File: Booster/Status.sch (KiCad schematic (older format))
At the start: 33 parts, among them J601 StatusLED, P601 ~OVERCURRENT_OUT, P602 ~OVERCURRENT_OUT_OP, P603 MSTR_SW, P604 MSTR_SW_OUT, P605 MSTR_SW_OUT_OP, P606 ~DRIVER_ENABLE_OUT_OP, P607 ~DRIVER_ENABLE_OUT, Q601 BC807-40, Q602 BC807-40, Q603 BC807-40, Q604 BC817-40, SW601 MSTR_SW, U504 74HC08, U602 PC817, U603 PC817, U604 PC817

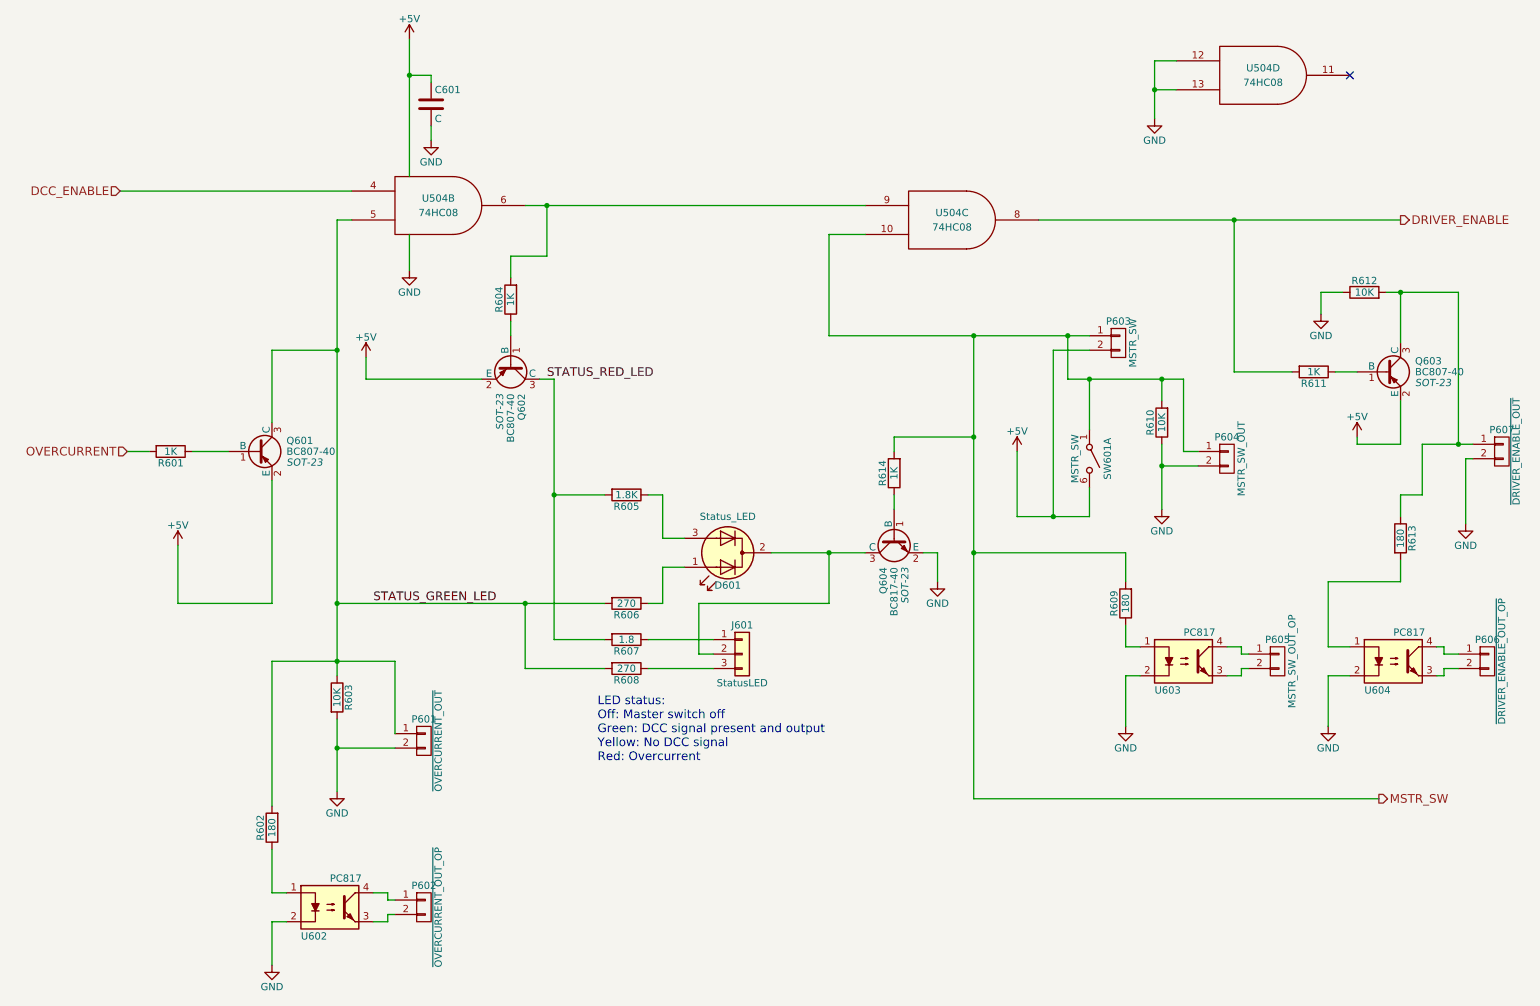
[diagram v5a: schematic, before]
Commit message: Assigned footprints & minor adjustments.
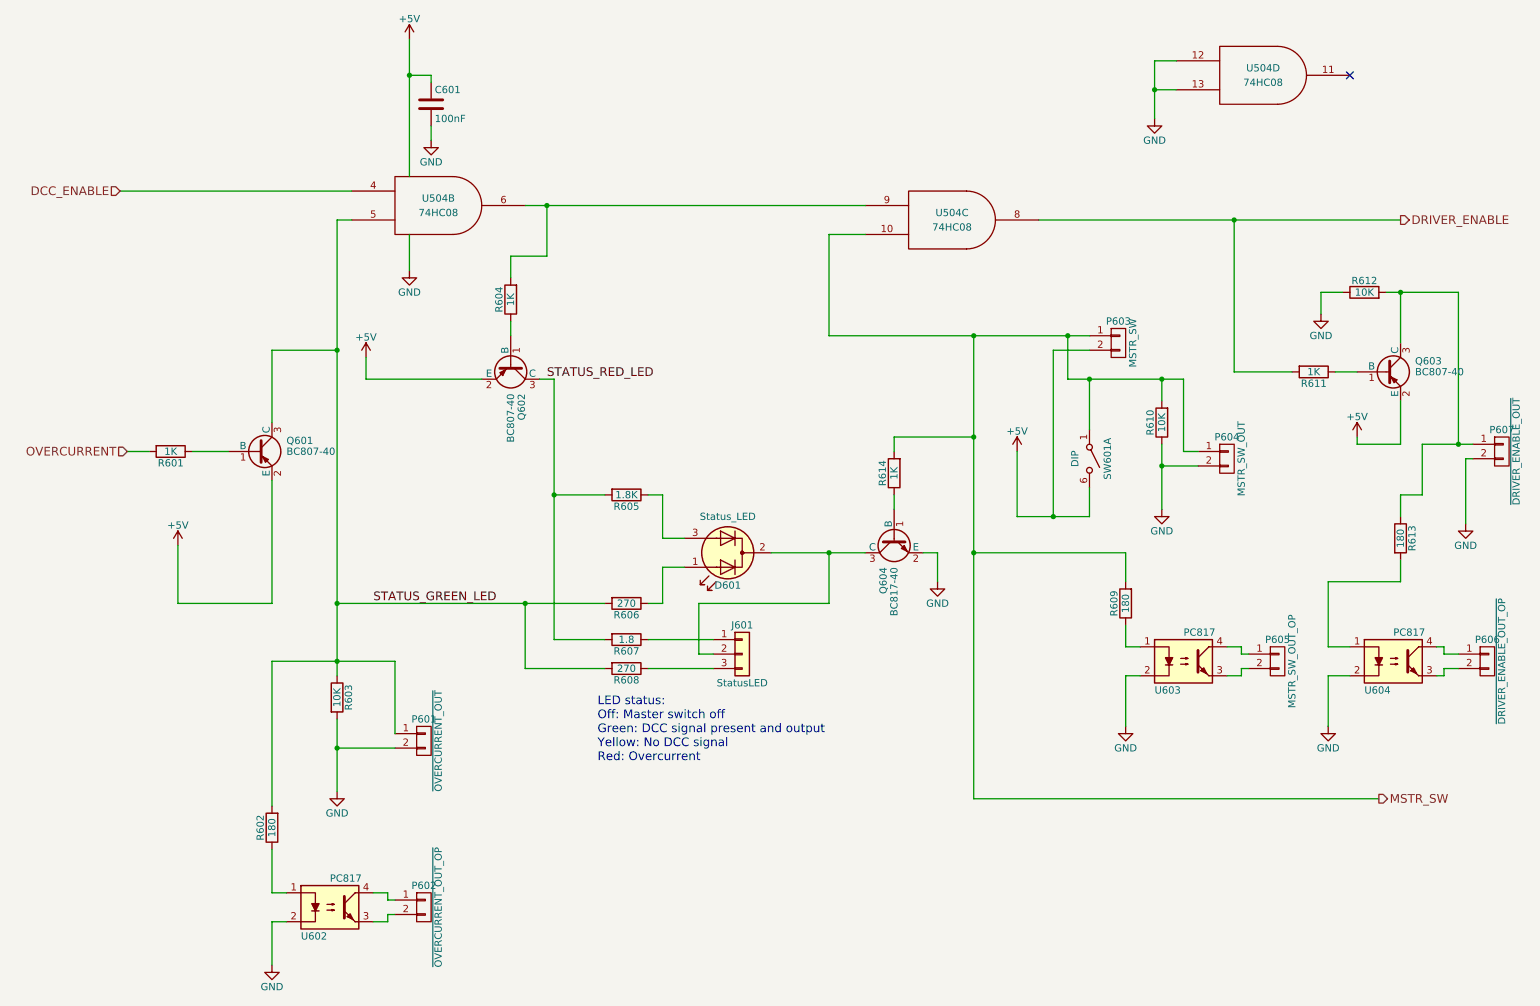
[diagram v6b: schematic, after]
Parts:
- C601: value C -> 100nF; footprint (none) -> Capacitors_SMD:C_0805
- D601: footprint (none) -> LEDs:LED_D3.0mm-3
- J601: footprint (none) -> Connectors_JST:JST_XH_B03B-XH-A_03x2.50mm_Straight
- P601, P602, P603, P604, P605, P606, P607: footprint (none) -> Connectors_JST:JST_XH_B02B-XH-A_02x2.50mm_Straight
- Q601, Q602, Q603, Q604: footprint SOT-23 -> TO_SOT_Packages_SMD:SOT-23
- R601, R602, R603, R604, R605, R606, R607, R608, R609, R610, R611, R612, R613, R614: footprint (none) -> Resistors_SMD:R_0805
- SW601: value MSTR_SW -> DIP; footprint (none) -> Buttons_Switches_THT:SW_DIP_x3_W7.62mm_Slide
- U504: footprint (none) -> SMD_Packages:SOIC-14_N

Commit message: Starting to add traces. Minor schematic changes to aid routing.
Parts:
- U602, U603, U604: footprint Housings_DIP:DIP-4_W7.62mm -> Housings_DIP:SMDIP-4_W9.53mm_Clearance8mm
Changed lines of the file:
@@
 $EndComp
 $Comp
-L +5V #PWR039
+L +5V #PWR609
 U 1 1 5A093F5C
 P 7600 3650
-F 0 "#PWR039" H 7600 3500 50  0001 C CNN
+F 0 "#PWR609" H 7600 3500 50  0001 C CNN
 F 1 "+5V" H 7600 3790 50  0000 C CNN
 F 2 "" H 7600 3650 50  0001 C CNN
@@
 $EndComp
 $Comp
-L +5V #PWR040
+L +5V #PWR601
 U 1 1 5A0BE54E
 P 1800 4300
-F 0 "#PWR040" H 1800 4150 50  0001 C CNN
+F 0 "#PWR601" H 1800 4150 50  0001 C CNN
 F 1 "+5V" H 1800 4440 50  0000 C CNN
 F 2 "" H 1800 4300 50  0001 C CNN
@@
 $EndComp
 $Comp
-L GND #PWR041
+L GND #PWR616
 U 1 1 5A0E0264
 P 10700 4150
-F 0 "#PWR041" H 10700 3900 50  0001 C CNN
+F 0 "#PWR616" H 10700 3900 50  0001 C CNN
 F 1 "GND" H 10700 4000 50  0000 C CNN
 F 2 "" H 10700 4150 50  0001 C CNN
@@
 $EndComp
 $Comp
-L +5V #PWR042
+L +5V #PWR615
 U 1 1 5A0E94CC
 P 9950 3550
-F 0 "#PWR042" H 9950 3400 50  0001 C CNN
+F 0 "#PWR615" H 9950 3400 50  0001 C CNN
 F 1 "+5V" H 9950 3690 50  0000 C CNN
 F 2 "" H 9950 3550 50  0001 C CNN
@@
 $EndComp
 $Comp
-L GND #PWR043
+L GND #PWR613
 U 1 1 5A0E9688
 P 9700 2700
-F 0 "#PWR043" H 9700 2450 50  0001 C CNN
+F 0 "#PWR613" H 9700 2450 50  0001 C CNN
 F 1 "GND" H 9700 2550 50  0000 C CNN
 F 2 "" H 9700 2700 50  0001 C CNN
@@
 $EndComp
 $Comp
-L GND #PWR044
+L GND #PWR603
 U 1 1 5A0E995B
 P 2900 6000
-F 0 "#PWR044" H 2900 5750 50  0001 C CNN
+F 0 "#PWR603" H 2900 5750 50  0001 C CNN
 F 1 "GND" H 2900 5850 50  0000 C CNN
 F 2 "" H 2900 6000 50  0001 C CNN
@@
 $EndComp
 $Comp
-L GND #PWR045
+L GND #PWR612
 U 1 1 5A094169
 P 8600 4050
-F 0 "#PWR045" H 8600 3800 50  0001 C CNN
+F 0 "#PWR612" H 8600 3800 50  0001 C CNN
 F 1 "GND" H 8600 3900 50  0000 C CNN
 F 2 "" H 8600 4050 50  0001 C CNN
@@
 F 0 "U604" H 10000 4900 50  0000 L CNN
 F 1 "PC817" H 10200 5300 50  0000 L CNN
-F 2 "Housings_DIP:DIP-4_W7.62mm" H 10000 4900 50  0001 L CIN
+F 2 "Housings_DIP:SMDIP-4_W9.53mm_Clearance8mm" H 10000 4900 50  0001 L CIN
 F 3 "" H 10200 5100 50  0001 L CNN
 	1    10200 5100
@@
 $EndComp
 $Comp
-L GND #PWR046
+L GND #PWR614
 U 1 1 5A0EDD5D
 P 9750 5550
-F 0 "#PWR046" H 9750 5300 50  0001 C CNN
+F 0 "#PWR614" H 9750 5300 50  0001 C CNN
 F 1 "GND" H 9750 5400 50  0000 C CNN
 F 2 "" H 9750 5550 50  0001 C CNN
@@
 F 0 "U603" H 8550 4900 50  0000 L CNN
 F 1 "PC817" H 8750 5300 50  0000 L CNN
-F 2 "Housings_DIP:DIP-4_W7.62mm" H 8550 4900 50  0001 L CIN
+F 2 "Housings_DIP:SMDIP-4_W9.53mm_Clearance8mm" H 8550 4900 50  0001 L CIN
 F 3 "" H 8750 5100 50  0001 L CNN
 	1    8750 5100
@@
 $EndComp
 $Comp
-L GND #PWR047
+L GND #PWR610
 U 1 1 5A0EE132
 P 8350 5550
-F 0 "#PWR047" H 8350 5300 50  0001 C CNN
+F 0 "#PWR610" H 8350 5300 50  0001 C CNN
 F 1 "GND" H 8350 5400 50  0000 C CNN
 F 2 "" H 8350 5550 50  0001 C CNN
@@
 F 0 "U602" H 2650 6600 50  0000 L CNN
 F 1 "PC817" H 2850 7000 50  0000 L CNN
-F 2 "Housings_DIP:DIP-4_W7.62mm" H 2650 6600 50  0001 L CIN
+F 2 "Housings_DIP:SMDIP-4_W9.53mm_Clearance8mm" H 2650 6600 50  0001 L CIN
 F 3 "" H 2850 6800 50  0001 L CNN
 	1    2850 6800
@@
 $EndComp
 $Comp
-L GND #PWR048
+L GND #PWR602
 U 1 1 5A0EF173
 P 2450 7200
-F 0 "#PWR048" H 2450 6950 50  0001 C CNN
+F 0 "#PWR602" H 2450 6950 50  0001 C CNN
 F 1 "GND" H 2450 7050 50  0000 C CNN
 F 2 "" H 2450 7200 50  0001 C CNN
@@
 $EndComp
 $Comp
-L +5V #PWR049
+L +5V #PWR604
 U 1 1 5A13183F
 P 3100 3000
-F 0 "#PWR049" H 3100 2850 50  0001 C CNN
+F 0 "#PWR604" H 3100 2850 50  0001 C CNN
 F 1 "+5V" H 3100 3140 50  0000 C CNN
 F 2 "" H 3100 3000 50  0001 C CNN
@@
 $EndComp
 $Comp
-L GND #PWR050
+L GND #PWR606
 U 1 1 5A1534F1
 P 3400 2400
-F 0 "#PWR050" H 3400 2150 50  0001 C CNN
+F 0 "#PWR606" H 3400 2150 50  0001 C CNN
 F 1 "GND" H 3400 2250 50  0000 C CNN
 F 2 "" H 3400 2400 50  0001 C CNN
@@
 $EndComp
 $Comp
-L +5V #PWR051
+L +5V #PWR605
 U 1 1 5A153603
 P 3400 800
-F 0 "#PWR051" H 3400 650 50  0001 C CNN
+F 0 "#PWR605" H 3400 650 50  0001 C CNN
 F 1 "+5V" H 3400 940 50  0000 C CNN
 F 2 "" H 3400 800 50  0001 C CNN
@@
 $EndComp
 $Comp
-L GND #PWR052
+L GND #PWR607
 U 1 1 5A1538DF
 P 3550 1500
-F 0 "#PWR052" H 3550 1250 50  0001 C CNN
+F 0 "#PWR607" H 3550 1250 50  0001 C CNN
 F 1 "GND" H 3550 1350 50  0000 C CNN
 F 2 "" H 3550 1500 50  0001 C CNN
@@
 Connection ~ 6300 4350
 $Comp
-L GND #PWR053
+L GND #PWR608
 U 1 1 5A3C3599
 P 7050 4550
-F 0 "#PWR053" H 7050 4300 50  0001 C CNN
+F 0 "#PWR608" H 7050 4300 50  0001 C CNN
 F 1 "GND" H 7050 4400 50  0000 C CNN
 F 2 "" H 7050 4550 50  0000 C CNN
@@
 Connection ~ 8550 1150
 $Comp
-L GND #PWR054
+L GND #PWR611
 U 1 1 5A3F671E
 P 8550 1350
-F 0 "#PWR054" H 8550 1100 50  0001 C CNN
+F 0 "#PWR611" H 8550 1100 50  0001 C CNN
 F 1 "GND" H 8550 1200 50  0000 C CNN
 F 2 "" H 8550 1350 50  0000 C CNN
